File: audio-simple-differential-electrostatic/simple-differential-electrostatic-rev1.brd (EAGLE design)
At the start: 152.4 x 127 mm, 81 parts, among them IC1 LT1115, IC2 LT1115, IC3 LT1115, IC4 LT1115, IC5 LM7915, IC6 LM7815, IC7 LM317T, IC8 LM317T, J1 LOUT, J2 VIN_PLATE, J3 ROUT, X1 LIN, X2 VIN_OPAMP, X3 RIN, X4 VIN_HEATER

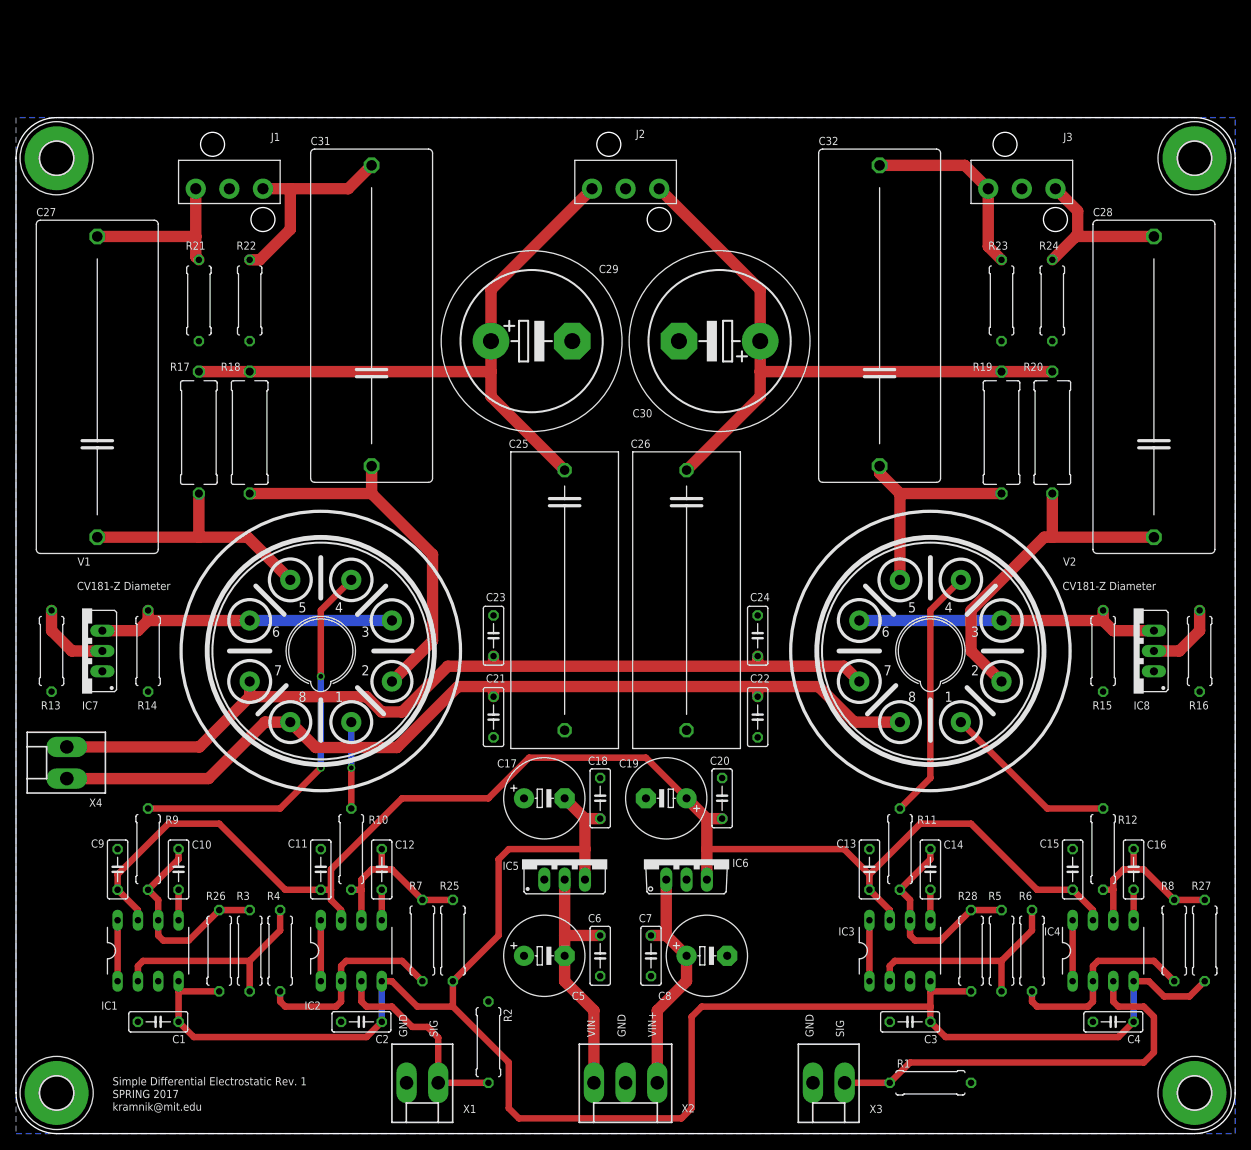
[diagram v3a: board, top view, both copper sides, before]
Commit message: Removed incorrect offset nulling shorts, ran renumber with new pulldown resistors
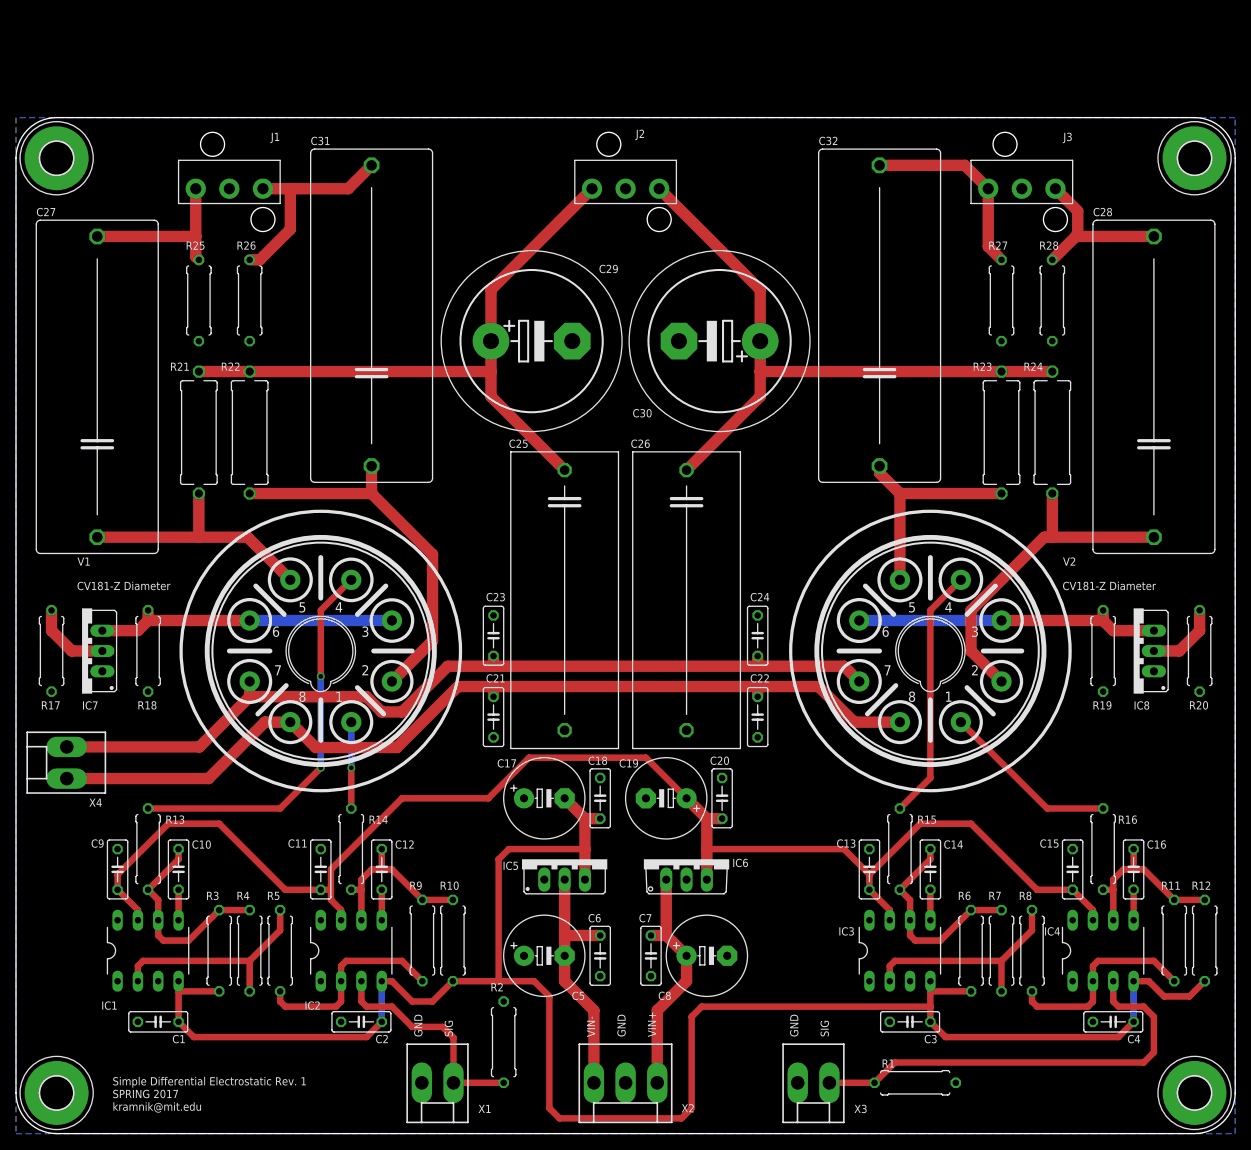
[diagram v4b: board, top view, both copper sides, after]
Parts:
- R10, R12: value 150R -> 10k
- R11, R9: value 150R -> 910R
- R13, R16: value 125R -> 150R
- R14, R15: value 685R -> 150R
- R17, R20: value 45k -> 125R; device rcl:P0613/15 -> rcl:0309/10
- R18, R19: value 45k -> 685R; device rcl:P0613/15 -> rcl:0309/10
- R21, R22, R23, R24: value 10M -> 45k; device rcl:0309/10 -> rcl:P0613/15
- R25, R26, R27, R28: value 10k -> 10M
- R3: value 1k -> 10k
- R4: value 100R -> 1k
- R5: value 1k -> 100R
- R6: value 100R -> 10k
- R7: value 910R -> 1k
- R8: value 910R -> 100R
- moved R5 90.2 mm to (33.0, 22.9)
- moved R25 86.1 mm to (22.9, 104.1)
- moved R27 83.9 mm to (123.2, 104.1)
- moved R28 81.9 mm to (129.5, 104.1)
- moved R26 81.4 mm to (29.2, 104.1)
- moved R7 72.4 mm to (123.2, 22.9)
- moved R11 36.1 mm to (144.8, 24.1), turned to 90 degrees
- moved R9 36.1 mm to (50.8, 24.1), turned to 90 degrees
- moved R14 35.5 mm to (41.9, 35.6), turned to 270 degrees
- moved R15 35.5 mm to (110.5, 35.6), turned to 270 degrees
- moved R20 32.9 mm to (148.0, 60.3)
- moved R17 32.9 mm to (4.45, 60.3)
- moved R18 30.1 mm to (16.5, 60.3)
- moved R19 30.1 mm to (135.9, 60.3)
- moved R16 27.5 mm to (135.9, 35.6), turned to 270 degrees
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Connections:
- removed net N$11: IC3.1, IC3.8
- removed net N$18: IC2.1, IC2.8
- removed net N$20: IC1.1, IC1.8
- removed net N$9: IC4.1, IC4.8
- net GND: now also R17.1, R18.1, R19.1, R20.1, R25.1, R26.1, R27.1, R28.1; no longer R13.1, R14.1, R15.1, R16.1, R21.1, R22.1, R23.1, R24.1
- net L_STATOR_N: now also R26.2; no longer R22.2
- net L_STATOR_P: now also R25.2; no longer R21.2
- net N$1: now also R19.2; no longer R15.2
- net N$10: now also R11.1; no longer R6.1
- net N$12: now also R21.1; no longer R17.1
- net N$13: now also R7.1, R8.2; no longer R5.1, R6.2
- net N$14: now also R15.2, R6.2, R7.2; no longer R11.2, R28.2, R5.2
- net N$15: now also R13.1; no longer R9.1
- net N$16: now also R14.1; no longer R10.1
- net N$17: now also R14.2, R9.2; no longer R25.2, R7.2
- net N$19: now also R5.1, R9.1; no longer R4.1, R7.1
- net N$2: now also R24.1; no longer R20.1
- net N$21: now also R4.1, R5.2; no longer R3.1, R4.2
- net N$22: now also R13.2, R4.2; no longer R26.2, R9.2
- net N$25: now also R20.2; no longer R16.2
- net N$3: now also R23.1; no longer R19.1
- net N$36: now also R17.2; no longer R13.2
- net N$4: now also R11.2, R16.2; no longer R27.2, R8.2
- net N$5: now also R18.2; no longer R14.2
- net N$6: now also R22.1; no longer R18.1
- net N$7: now also R15.1; no longer R11.1
- net N$8: now also R16.1; no longer R12.1
- net PP_N15V0_OPAMP: now also R10.1, R12.1, R3.1, R6.1; no longer R25.1, R26.1, R27.1, R28.1
- net PP_P450V_L_PLATE: now also R21.2, R22.2; no longer R17.2, R18.2
- net PP_P450V_R_PLATE: now also R23.2, R24.2; no longer R19.2, R20.2
- net R_STATOR_N: now also R28.2; no longer R24.2
- net R_STATOR_P: now also R27.2; no longer R23.2
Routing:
- net N$9: track 7.62 -> 0.00 mm
- net N$20: track 7.62 -> 0.00 mm
- net N$18: track 7.62 -> 0.00 mm
- net N$11: track 7.62 -> 0.00 mm
- net R_INPUT: track 53.1 -> 55.0 mm
- net L_INPUT: track 25.9 -> 27.8 mm
- net PP_N15V0_OPAMP: track 231.6 -> 233.0 mm
